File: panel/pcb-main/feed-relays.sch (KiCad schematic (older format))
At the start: 14 parts

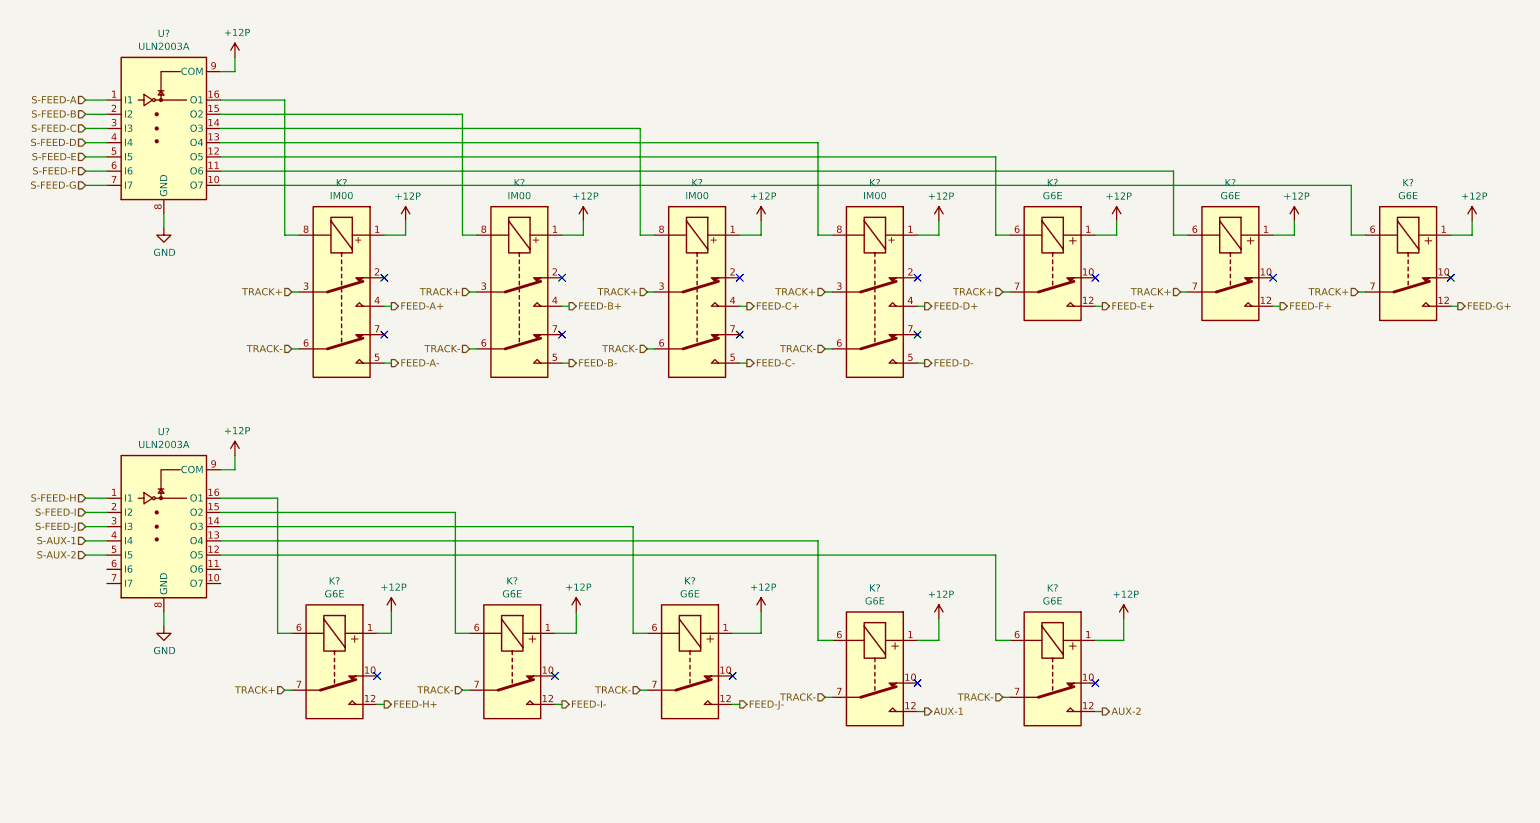
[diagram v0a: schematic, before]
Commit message: PCB Updates and added panel-fw project.
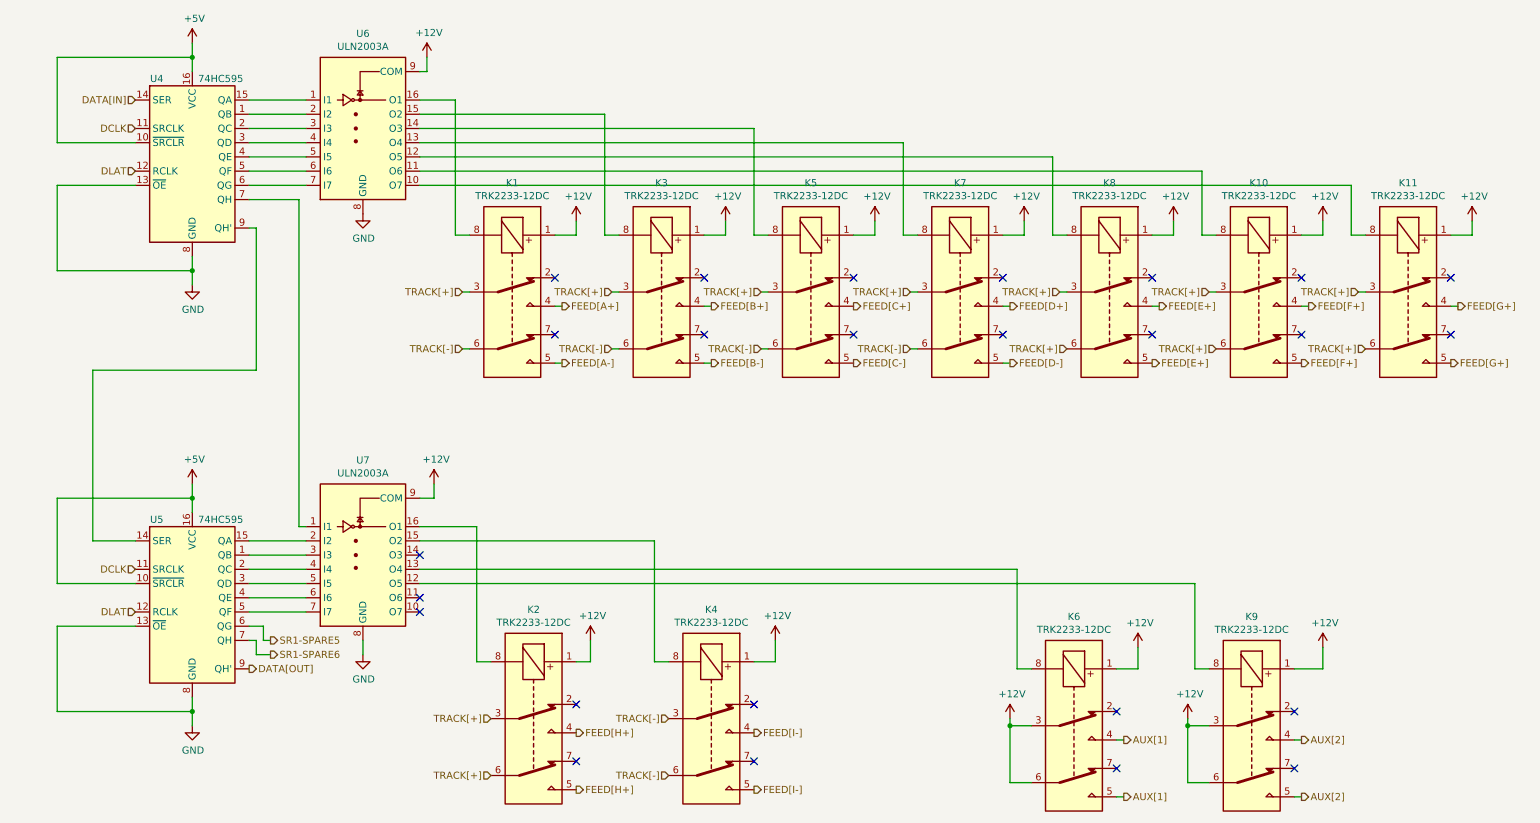
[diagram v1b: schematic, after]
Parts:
- removed K? (x8): G6E, Relay_THT:Relay_SPDT_Omron_G6E, symbol Relay:G6E
- added K10, K11, K2, K4, K6, K8, K9: TRK2233-12DC, carnivalben:TRK22X3-XXDC, symbol Relay:IM00
- added U4, U5: 74HC595, Housings_DIP:DIP-16_W7.62mm_LongPads, symbol 74xx:74HC595
- K1, K3, K5, K7: renamed from K?; value IM00 -> TRK2233-12DC; footprint (none) -> carnivalben:TRK22X3-XXDC
- U6, U7: renamed from U?; footprint (none) -> Housings_DIP:DIP-16_W7.62mm_LongPads
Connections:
- net GND: now also U4.13 (~OE), U4.8 (GND), U5.13 (~OE), U5.8 (GND)
- net at U6.12 (O5): now also K8.8
- net at U6.11 (O6): now also K10.8
- net at U6.10 (O7): now also K11.8
- net at U7.16 (O1): now also K2.8
- net at U7.15 (O2): now also K4.8
- net at U7.12 (O5): now also K9.8
- net at U7.13 (O4): now also K6.8
- net at U7.6 (I6): now also U5.4 (QE)
- net at U7.7 (I7): now also U5.5 (QF)
- net +12P renamed +12V
- net +12V: now also K10.1, K11.1, K2.1, K4.1, K6.1, K6.3, K6.6, K8.1, K9.1, K9.3, K9.6
- net FEED-A+ renamed FEED[A+]
- net FEED-A- renamed FEED[A-]
- net FEED-B+ renamed FEED[B+]
- net FEED-B- renamed FEED[B-]
- net FEED-C+ renamed FEED[C+]
- net FEED-C- renamed FEED[C-]
- net FEED-D+ renamed FEED[D+]
- net FEED-D- renamed FEED[D-]
- net S-AUX-1: no longer names the net of U7.4 (I4)
- net S-AUX-1: now also U5.2 (QC)
- net S-AUX-2: no longer names the net of U7.5 (I5)
- net S-AUX-2: now also U5.3 (QD)
- net S-FEED-A: no longer names the net of U6.1 (I1)
- net S-FEED-A: now also U4.15 (QA)
- net S-FEED-B: no longer names the net of U6.2 (I2)
- net S-FEED-B: now also U4.1 (QB)
- net S-FEED-C: no longer names the net of U6.3 (I3)
- net S-FEED-C: now also U4.2 (QC)
- net S-FEED-D: no longer names the net of U6.4 (I4)
- net S-FEED-D: now also U4.3 (QD)
- net S-FEED-E: no longer names the net of U6.5 (I5)
- net S-FEED-E: now also U4.4 (QE)
- net S-FEED-F: no longer names the net of U6.6 (I6)
- net S-FEED-F: now also U4.5 (QF)
- net S-FEED-G: no longer names the net of U6.7 (I7)
- net S-FEED-G: now also U4.6 (QG)
- net S-FEED-H: no longer names the net of U7.1 (I1)
- net S-FEED-H: now also U4.7 (QH)
- net S-FEED-I: no longer names the net of U7.2 (I2)
- net S-FEED-I: now also U5.15 (QA)
- net S-FEED-J: no longer names the net of U7.3 (I3)
- net S-FEED-J: now also U5.1 (QB)
- net TRACK+ renamed TRACK[+]
- net TRACK[+]: now also K10.3, K10.6, K11.3, K11.6, K2.3, K2.6, K8.3, K8.6
- net TRACK- renamed TRACK[-]
- net TRACK[-]: now also K4.3, K4.6
- new net: U4.9 (QH'), U5.14 (SER)
- new net +5V: U4.10 (~SRCLR), U4.16 (VCC), U5.10 (~SRCLR), U5.16 (VCC)
- new net AUX[1]: K6.4, K6.5
- new net AUX[2]: K9.4, K9.5
- new net DATA[IN]: U4.14 (SER)
- new net DATA[OUT]: U5.9 (QH')
- new net DCLK: U4.11 (SRCLK), U5.11 (SRCLK)
- new net DLAT: U4.12 (RCLK), U5.12 (RCLK)
- new net FEED[E+]: K8.4, K8.5
- new net FEED[F+]: K10.4, K10.5
- new net FEED[G+]: K11.4, K11.5
- new net FEED[H+]: K2.4, K2.5
- new net FEED[I-]: K4.4, K4.5
- new net SR1-SPARE5: U5.6 (QG)
- new net SR1-SPARE6: U5.7 (QH)
- no-connect marks 16 -> 25
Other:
- moved on the sheet: K1, K3, K5, K7, U6, U7
